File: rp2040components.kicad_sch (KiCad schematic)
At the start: 16 parts, among them P2 Header 1.27mm 2x5 PTH, P3 Header 3, U8 W25Q128JVSIQTR, Y1 X322512MSB4SI

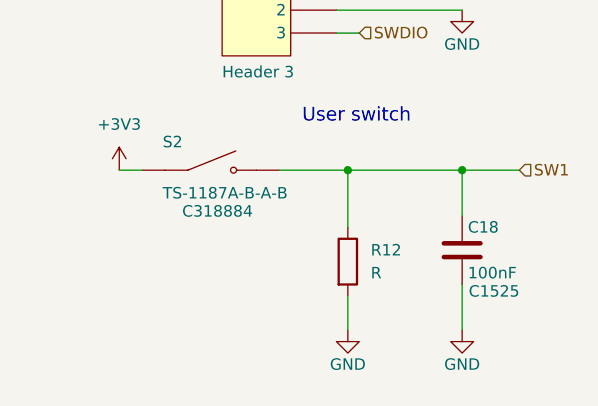
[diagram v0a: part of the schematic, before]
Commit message: Add symbol/footprint library linkages.
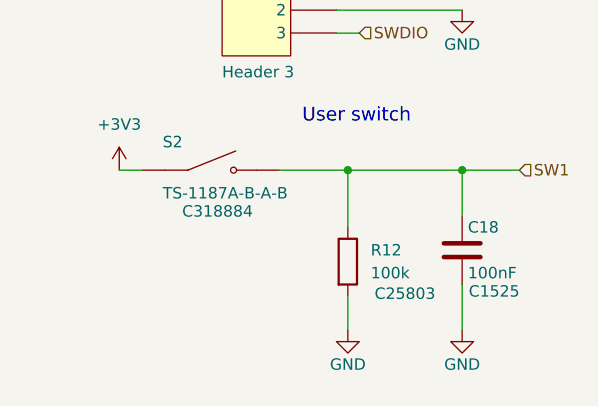
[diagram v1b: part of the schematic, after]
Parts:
- R12: value R -> 100k; footprint (none) -> Resistor_SMD:R_0201_0603Metric; LCSC PN (none) -> C25803
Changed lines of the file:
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@@
 			)
 		)
-		(property "Value" "R"
+		(property "Value" "100k"
 			(at 245.11 118.1099 0)
 			(show_name no)
@@
 			)
 		)
-		(property "Footprint" ""
+		(property "Footprint" "Resistor_SMD:R_0201_0603Metric"
 			(at 240.792 116.84 90)
 			(hide yes)
@@
 			)
 		)
-		(property "LCSC PN" ""
+		(property "LCSC PN" "C25803 "
 			(at 248.92 120.396 0)
 			(show_name no)

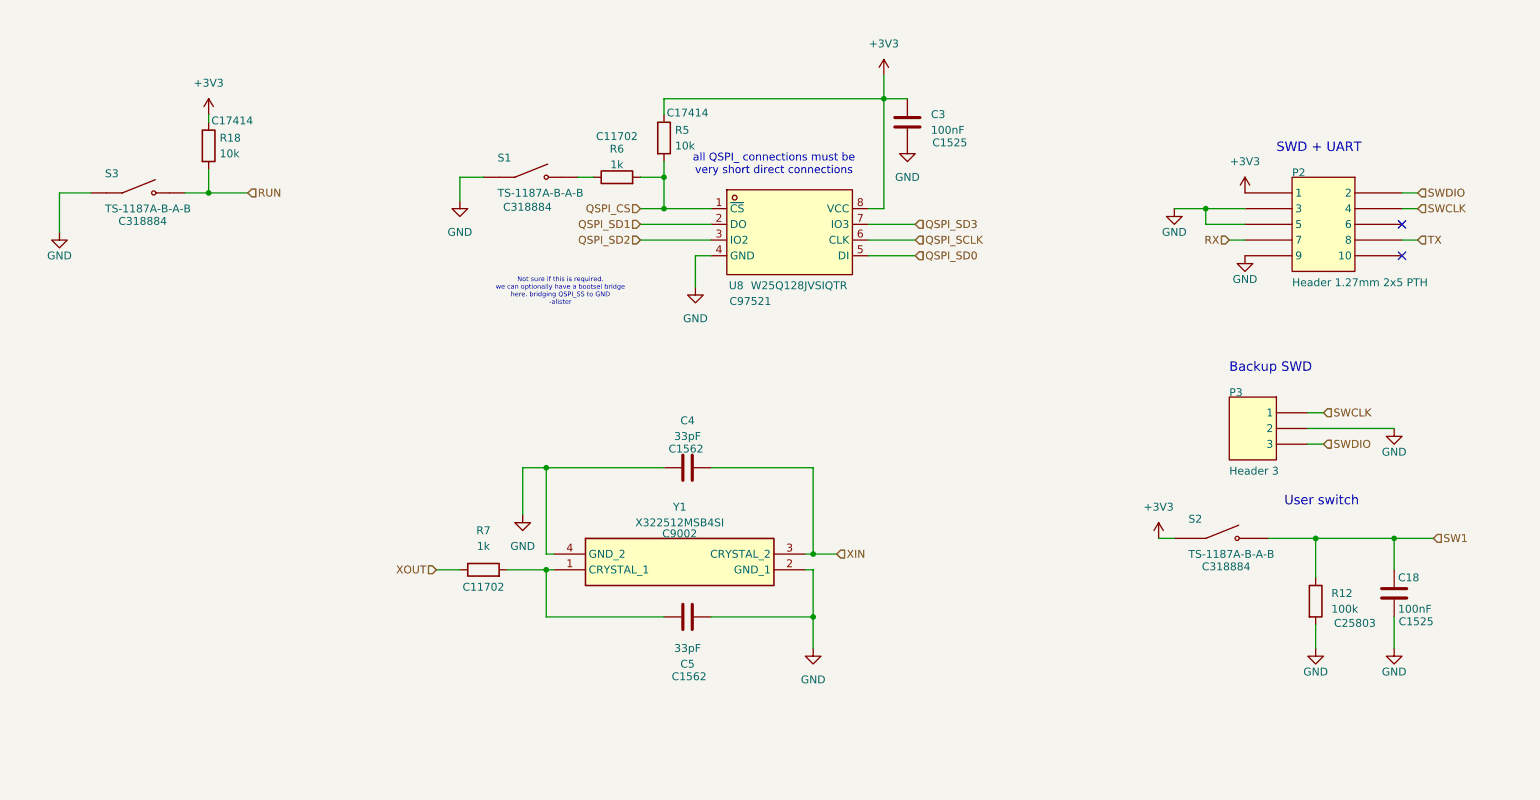
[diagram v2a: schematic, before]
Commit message: add door limit switch connector and hardware debounce.
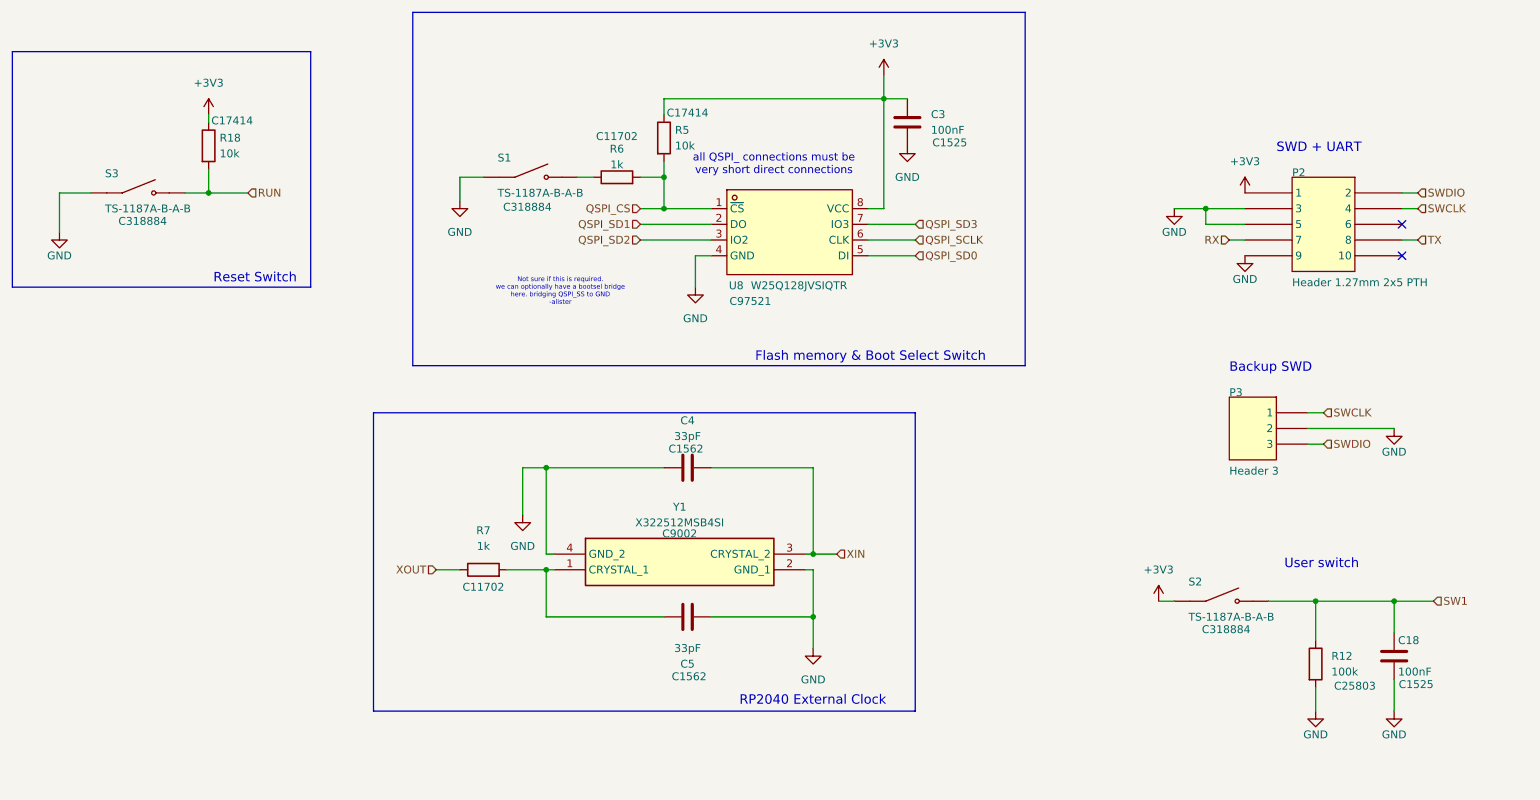
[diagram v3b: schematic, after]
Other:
- note added: "Flash memory & Boot Select Switch"
- note added: "RP2040 External Clock"
- note added: "Reset Switch"
- moved on the sheet: C18, R12, S2

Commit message: Update sheet naming
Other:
- company: (none) -> Alister, Damien, Nils
- title: RP2040 Components -> CC3501 Design Project
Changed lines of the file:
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@@
 	(paper "A4")
 	(title_block
-		(title "RP2040 Components")
+		(title "CC3501 Design Project")
+		(date "2026-06-22")
+		(rev "1")
+		(company "Alister, Damien, Nils")
 	)
 	(rectangle

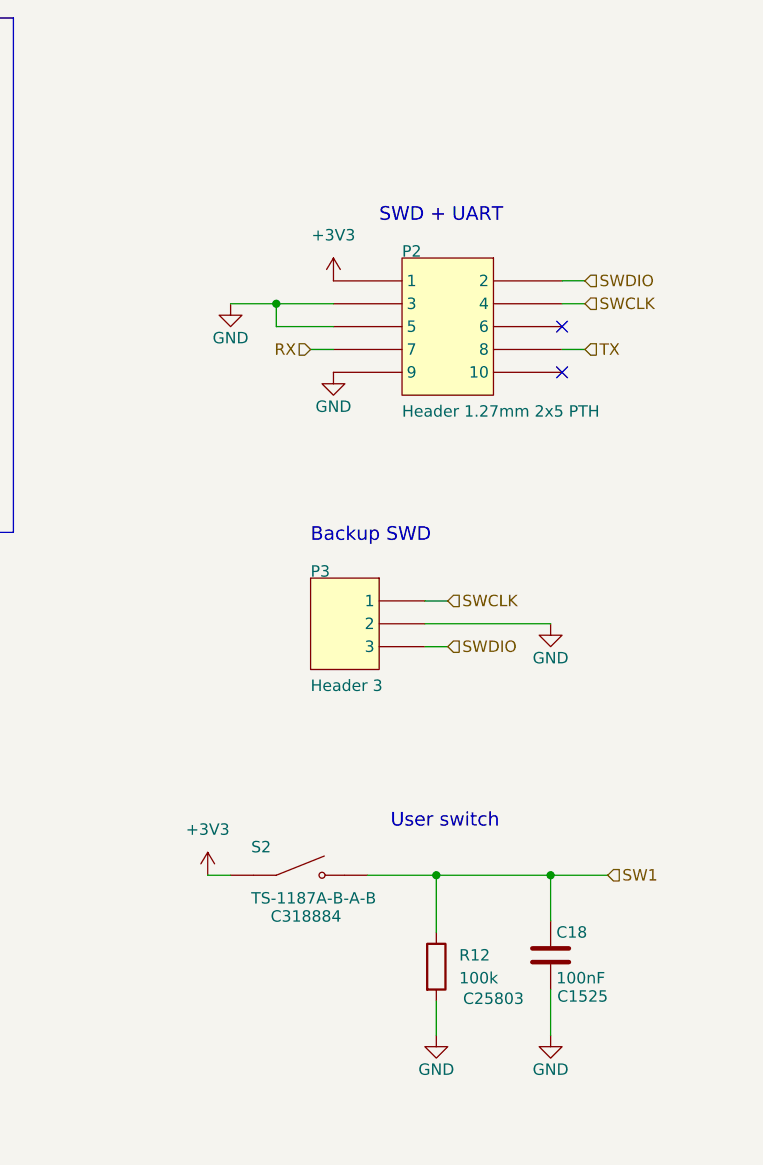
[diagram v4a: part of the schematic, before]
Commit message: add boxes around system blocks with labels
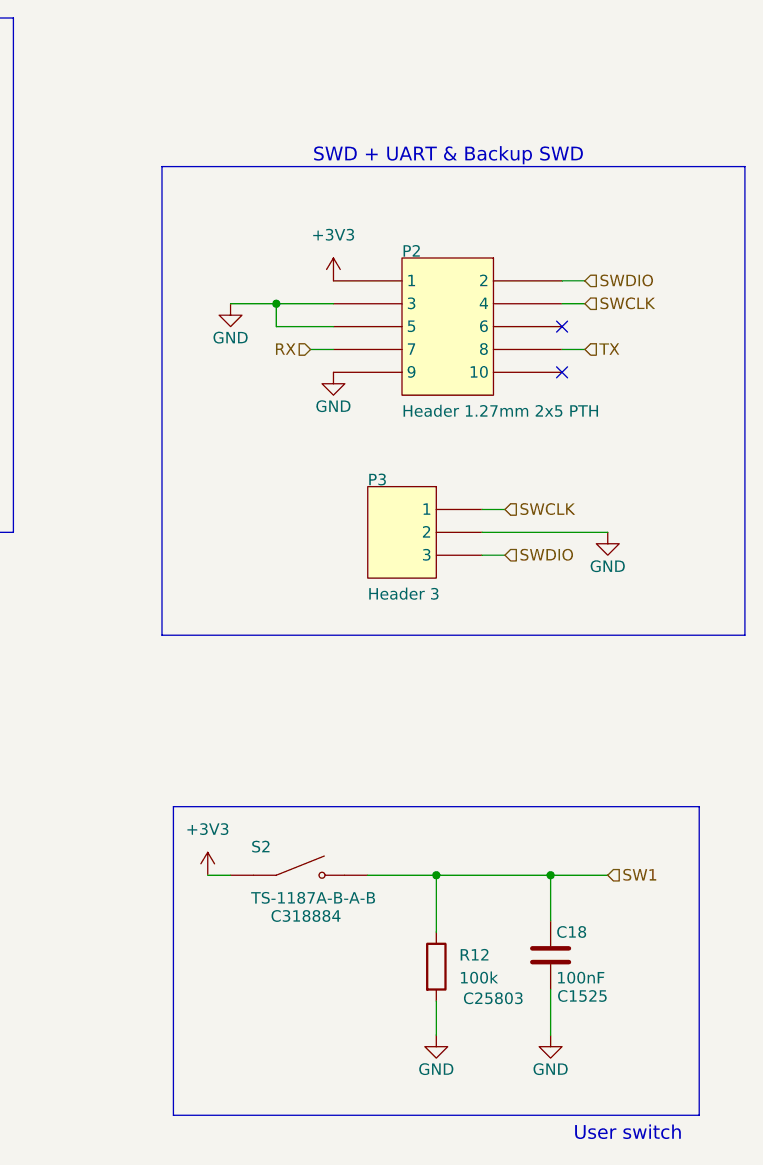
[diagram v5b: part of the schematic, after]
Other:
- note added: "SWD + UART & Backup SWD"
- note removed: "Backup SWD"
- note removed: "SWD + UART"
- moved on the sheet: P3
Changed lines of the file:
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@@
 	)
 	(rectangle
+		(start 212.09 38.1)
+		(end 276.86 90.17)
+		(stroke
+			(width 0)
+			(type default)
+		)
+		(fill
+			(type none)
+		)
+	)
+	(rectangle
+		(start 213.36 109.22)
+		(end 271.78 143.51)
+		(stroke
+			(width 0)
+			(type default)
+		)
+		(fill
+			(type none)
+		)
+	)
+	(rectangle
 		(start 96.52 21.59)
 		(end 195.58 78.74)
@@
 		)
 	)
-	(text "SWD + UART"
+	(text "SWD + UART & Backup SWD"
 		(exclude_from_sim no)
-		(at 236.22 44.45 0)
+		(at 228.854 37.846 0)
 		(effects
 			(font
@@
 		)
 	)
-	(text "Backup SWD"
+	(text ""
 		(exclude_from_sim no)
-		(at 228.6 80.01 0)
+		(at 234.95 69.85 0)
 		(effects
 			(font
@@
 	(text "User switch"
 		(exclude_from_sim no)
-		(at 237.49 111.76 0)
+		(at 257.81 146.558 0)
 		(effects
 			(font
@@
 	(wire
 		(pts
-			(xy 241.3 88.9) (xy 255.27 88.9)
+			(xy 247.65 78.74) (xy 261.62 78.74)
 		)
 		(stroke
@@
 	(wire
 		(pts
-			(xy 241.3 91.44) (xy 243.84 91.44)
+			(xy 247.65 81.28) (xy 250.19 81.28)
 		)
 		(stroke
@@
 	(wire
 		(pts
-			(xy 241.3 86.36) (xy 243.84 86.36)
+			(xy 247.65 76.2) (xy 250.19 76.2)
 		)
 		(stroke
@@
 	(hierarchical_label "SWDIO"
 		(shape input)
-		(at 243.84 91.44 0)
+		(at 250.19 81.28 0)
 		(effects
 			(font
@@
 	(hierarchical_label "SWCLK"
 		(shape input)
-		(at 243.84 86.36 0)
+		(at 250.19 76.2 0)
 		(effects
 			(font
@@
 	(symbol
 		(lib_id "power:GND")
-		(at 255.27 88.9 0)
+		(at 261.62 78.74 0)
 		(unit 1)
 		(body_style 1)
@@
 		(dnp no)
 		(property "Reference" "#PWR136"
-			(at 255.27 95.25 0)
+			(at 261.62 85.09 0)
 			(hide yes)
 			(show_name no)
@@
 		)
 		(property "Value" "GND"
-			(at 255.27 92.71 0)
+			(at 261.62 82.55 0)
 			(show_name no)
 			(do_not_autoplace no)
@@
 		)
 		(property "Footprint" ""
-			(at 255.27 88.9 0)
+			(at 261.62 78.74 0)
 			(hide yes)
 			(show_name no)
@@
 		)
 		(property "Datasheet" ""
-			(at 255.27 88.9 0)
+			(at 261.62 78.74 0)
 			(hide yes)
 			(show_name no)
@@
 		)
 		(property "Description" "Power symbol creates a global label with name \"GND\" , ground"
-			(at 255.27 88.9 0)
+			(at 261.62 78.74 0)
 			(hide yes)
 			(show_name no)
@@
 	(symbol
 		(lib_id "Miscellaneous Connectors:root_0_mirrored_Header 3_Miscellaneous Connectors.IntLib")
-		(at 236.22 83.82 0)
+		(at 242.57 73.66 0)
 		(unit 1)
 		(body_style 1)
@@
 		(dnp no)
 		(property "Reference" "P3"
-			(at 228.6 83.82 0)
+			(at 234.95 73.66 0)
 			(show_name no)
 			(do_not_autoplace no)
@@
 		)
 		(property "Value" "Header 3"
-			(at 228.6 96.52 0)
+			(at 234.95 86.36 0)
 			(show_name no)
 			(do_not_autoplace no)
@@
 		)
 		(property "Footprint" "Connector_PinHeader_2.54mm:PinHeader_1x03_P2.54mm_Vertical"
-			(at 236.22 83.82 0)
+			(at 242.57 73.66 0)
 			(hide yes)
 			(show_name no)
@@
 		)
 		(property "Datasheet" ""
-			(at 236.22 83.82 0)
+			(at 242.57 73.66 0)
 			(hide yes)
 			(show_name no)
@@
 		)
 		(property "Description" "Header, 3-Pin"
-			(at 236.22 83.82 0)
+			(at 242.57 73.66 0)
 			(hide yes)
 			(show_name no)
@@
 		)
 		(property "LATESTREVISIONDATE" "17-Jul-2002"
-			(at 228.6 83.82 0)
+			(at 234.95 73.66 0)
 			(hide yes)
 			(show_name no)
@@
 		)
 		(property "LATESTREVISIONNOTE" "Re-released for DXP Platform."
-			(at 228.6 83.82 0)
+			(at 234.95 73.66 0)
 			(hide yes)
 			(show_name no)
@@
 		)
 		(property "PUBLISHER" "Altium Limited"
-			(at 228.6 83.82 0)
+			(at 234.95 73.66 0)
 			(hide yes)
 			(show_name no)
@@
 		)
 		(property "CAPACITANCE" ""
-			(at 236.22 83.82 0)
+			(at 242.57 73.66 0)
 			(hide yes)
 			(show_name no)
@@
 		)
 		(property "CASE SIZE/DIMENSION" ""
-			(at 236.22 83.82 0)
+			(at 242.57 73.66 0)
 			(hide yes)
 			(show_name no)
@@
 		)
 		(property "DATASHEET URL" ""
-			(at 236.22 83.82 0)
+			(at 242.57 73.66 0)
 			(hide yes)
 			(show_name no)
@@
 		)
 		(property "DATASHEET VERSION" ""
-			(at 236.22 83.82 0)
+			(at 242.57 73.66 0)
 			(hide yes)
 			(show_name no)
@@
 		)
 		(property "DIELECTRIC" ""
-			(at 236.22 83.82 0)
+			(at 242.57 73.66 0)
 			(hide yes)
 			(show_name no)
@@
 		)
 		(property "MANUFACTURER URL" ""
-			(at 236.22 83.82 0)
+			(at 242.57 73.66 0)
 			(hide yes)
 			(show_name no)
@@
 		)
 		(property "RATED VOLTAGE" ""
-			(at 236.22 83.82 0)
+			(at 242.57 73.66 0)
 			(hide yes)
 			(show_name no)
@@
 		)
 		(property "TOLERANCE (%)" ""
-			(at 236.22 83.82 0)
+			(at 242.57 73.66 0)
 			(hide yes)
 			(show_name no)
@@
 		)
 		(property "KLC_S3.3" ""
-			(at 236.22 83.82 0)
+			(at 242.57 73.66 0)
 			(hide yes)
 			(show_name no)
@@
 		)
 		(property "KLC_S4.1" ""
-			(at 236.22 83.82 0)
+			(at 242.57 73.66 0)
 			(hide yes)
 			(show_name no)
@@
 		)
 		(property "CASE CODE (IMPERIAL)" ""
-			(at 236.22 83.82 0)
+			(at 242.57 73.66 0)
 			(hide yes)
 			(show_name no)
@@
 		)
 		(property "CASE CODE (METRIC)" ""
-			(at 236.22 83.82 0)
+			(at 242.57 73.66 0)
 			(hide yes)
 			(show_name no)
@@
 		)
 		(property "CASE/PACKAGE" ""
-			(at 236.22 83.82 0)
+			(at 242.57 73.66 0)
 			(hide yes)
 			(show_name no)
@@
 		)
 		(property "COMPOSITION" ""
-			(at 236.22 83.82 0)
+			(at 242.57 73.66 0)
 			(hide yes)
 			(show_name no)
@@
 		)
 		(property "CONTACT PLATING" ""
-			(at 236.22 83.82 0)
+			(at 242.57 73.66 0)
 			(hide yes)
 			(show_name no)
@@
 		)
 		(property "DEPTH" ""
-			(at 236.22 83.82 0)
+			(at 242.57 73.66 0)
 			(hide yes)
 			(show_name no)
@@
 		)
 		(property "LEAD FREE" ""
-			(at 236.22 83.82 0)
+			(at 242.57 73.66 0)
 			(hide yes)
 			(show_name no)
@@
 		)
 		(property "LENGTH" ""
-			(at 236.22 83.82 0)
+			(at 242.57 73.66 0)
 			(hide yes)
 			(show_name no)
@@
 		)
 		(property "MAX OPERATING TEMPERATURE" ""
-			(at 236.22 83.82 0)
+			(at 242.57 73.66 0)
 			(hide yes)
 			(show_name no)
@@
 		)
 		(property "MILITARY STANDARD" ""
-			(at 236.22 83.82 0)
+			(at 242.57 73.66 0)
 			(hide yes)
 			(show_name no)
@@
 		)
 		(property "MIN OPERATING TEMPERATURE" ""
-			(at 236.22 83.82 0)
+			(at 242.57 73.66 0)
 			(hide yes)
 			(show_name no)
@@
 		)
 		(property "MOUNT" ""
-			(at 236.22 83.82 0)
+			(at 242.57 73.66 0)
 			(hide yes)
 			(show_name no)
@@
 		)
 		(property "NUMBER OF PINS" ""
-			(at 236.22 83.82 0)
+			(at 242.57 73.66 0)
 			(hide yes)
 			(show_name no)
@@
 		)
 		(property "PACKAGE QUANTITY" ""
-			(at 236.22 83.82 0)
+			(at 242.57 73.66 0)
 			(hide yes)
 			(show_name no)
@@
 		)
 		(property "PACKAGING" ""
-			(at 236.22 83.82 0)
+			(at 242.57 73.66 0)
 			(hide yes)
 			(show_name no)
@@
 		)
 		(property "POWER RATING" ""
-			(at 236.22 83.82 0)
+			(at 242.57 73.66 0)
 			(hide yes)
 			(show_name no)
@@
 		)
 		(property "RADIATION HARDENING" ""
-			(at 236.22 83.82 0)
+			(at 242.57 73.66 0)
 			(hide yes)
 			(show_name no)
@@
 		)
 		(property "RESISTANCE" ""
-			(at 236.22 83.82 0)
+			(at 242.57 73.66 0)
 			(hide yes)
 			(show_name no)
@@
 		)
 		(property "TEMPERATURE COEFFICIENT" ""
-			(at 236.22 83.82 0)
+			(at 242.57 73.66 0)
 			(hide yes)
 			(show_name no)
@@
 		)
 		(property "TERMINATION" ""
-			(at 236.22 83.82 0)
+			(at 242.57 73.66 0)
 			(hide yes)
 			(show_name no)
@@
 		)
 		(property "TOLERANCE" ""
-			(at 236.22 83.82 0)
+			(at 242.57 73.66 0)
 			(hide yes)
 			(show_name no)
@@
 		)
 		(property "VOLTAGE RATING" ""
-			(at 236.22 83.82 0)
+			(at 242.57 73.66 0)
 			(hide yes)
 			(show_name no)
@@
 		)
 		(property "VOLTAGE RATING (DC)" ""
-			(at 236.22 83.82 0)
+			(at 242.57 73.66 0)
 			(hide yes)
 			(show_name no)
@@
 		)
 		(property "WEIGHT" ""
-			(at 236.22 83.82 0)
+			(at 242.57 73.66 0)
 			(hide yes)
 			(show_name no)
@@
 		)
 		(property "WIDTH" ""
-			(at 236.22 83.82 0)
+			(at 242.57 73.66 0)
 			(hide yes)
 			(show_name no)
